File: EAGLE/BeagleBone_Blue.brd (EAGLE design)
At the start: 86.4 x 54.6 mm, 305 parts, among them J2 SERVO_HEADERS_8X, M1 JST_ZH_2, M2 JST_ZH_2, M3 JST_ZH_2, M4 JST_ZH_2, Q1 MOSFET-N, U1 TCAN1051HV, U10 TXS0108ERGYR, U13 EMMC, U2 SN74LV1T126DBVR, U3 TPD4S012DRY, U4 TPD4S012DRY, U5 24LC_32AT-I/OT, U6 SN74LVC1G07_DCK_5, U7 WL1835MODGBMOCT, U9 TXS0108ERGYR, X2 SCHA5B0200, X3 USB1, X4 10118192-0001LF, Y1 24 MHz, Y2 32.768kHz

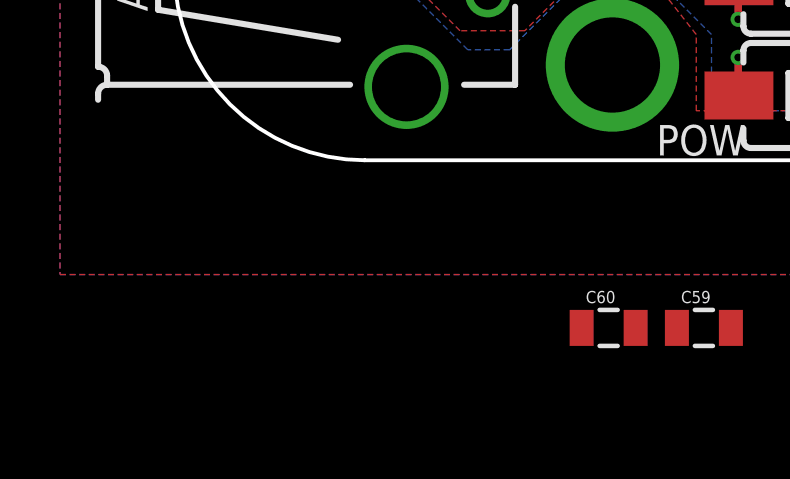
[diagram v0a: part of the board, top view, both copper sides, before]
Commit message: Added TPS2105 power mux for USB1 power.
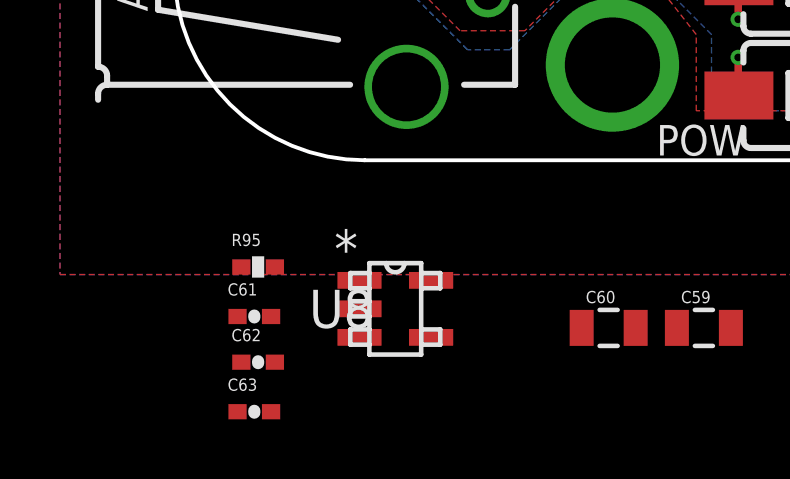
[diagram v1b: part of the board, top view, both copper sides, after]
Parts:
- added C61: 1uF, Strawson_Eagle_Lib:0402-CAP
- added C62, C63: 0.22uF, Strawson_Eagle_Lib:0402-CAP
- added R95: 100K, Strawson_Eagle_Lib:0402-RES
- added U8: TPS2105_DBV_5, BeagleBone_Blue:DBV5
- R119: value 0 -> 0, DNP
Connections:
- net 5.0V: now also C63.1, R95.2, U8.1, U8.5
- net GND: now also C61.1, C62.2, C63.2, R95.1, U8.2
- net SYS_5V: now also C62.1, U8.3
- net USB1_VBUS: now also C61.2, U8.4

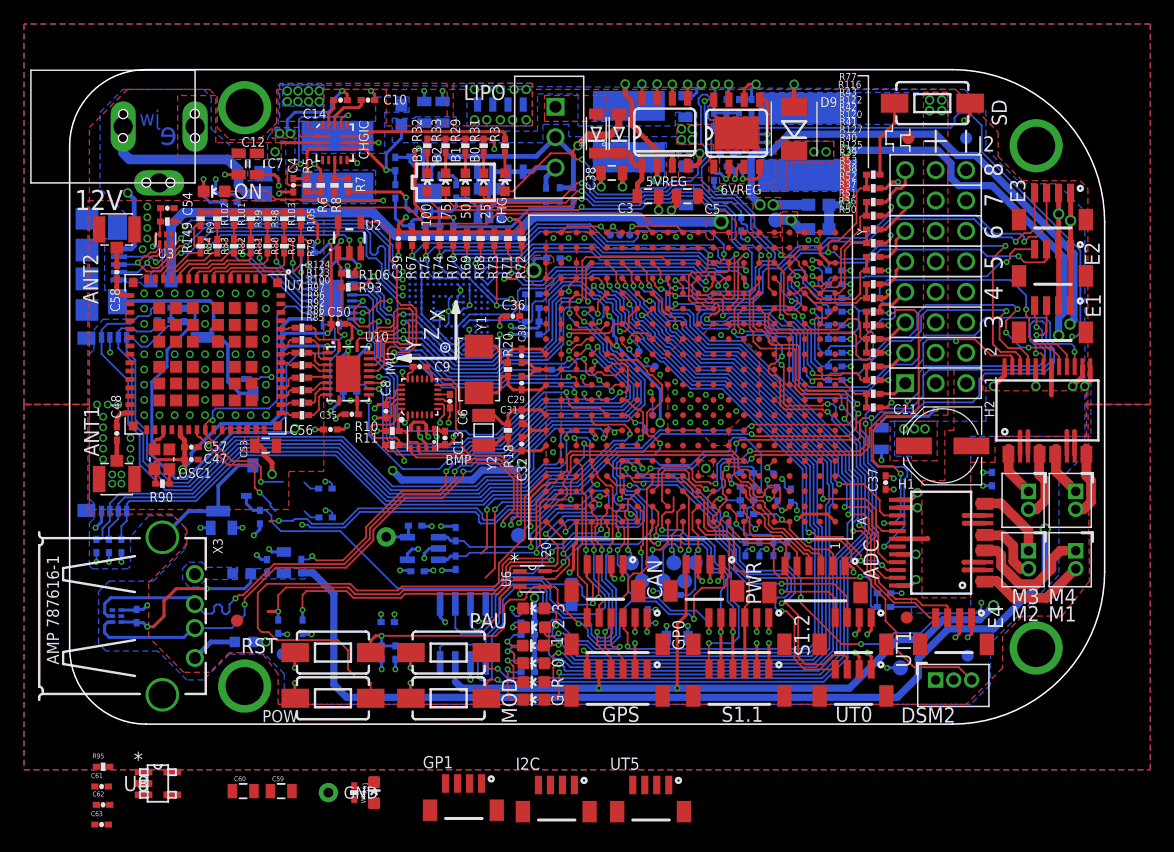
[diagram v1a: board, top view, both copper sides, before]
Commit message: Intermediate commit; Updated layout; Fixed TPS2105 footprint.
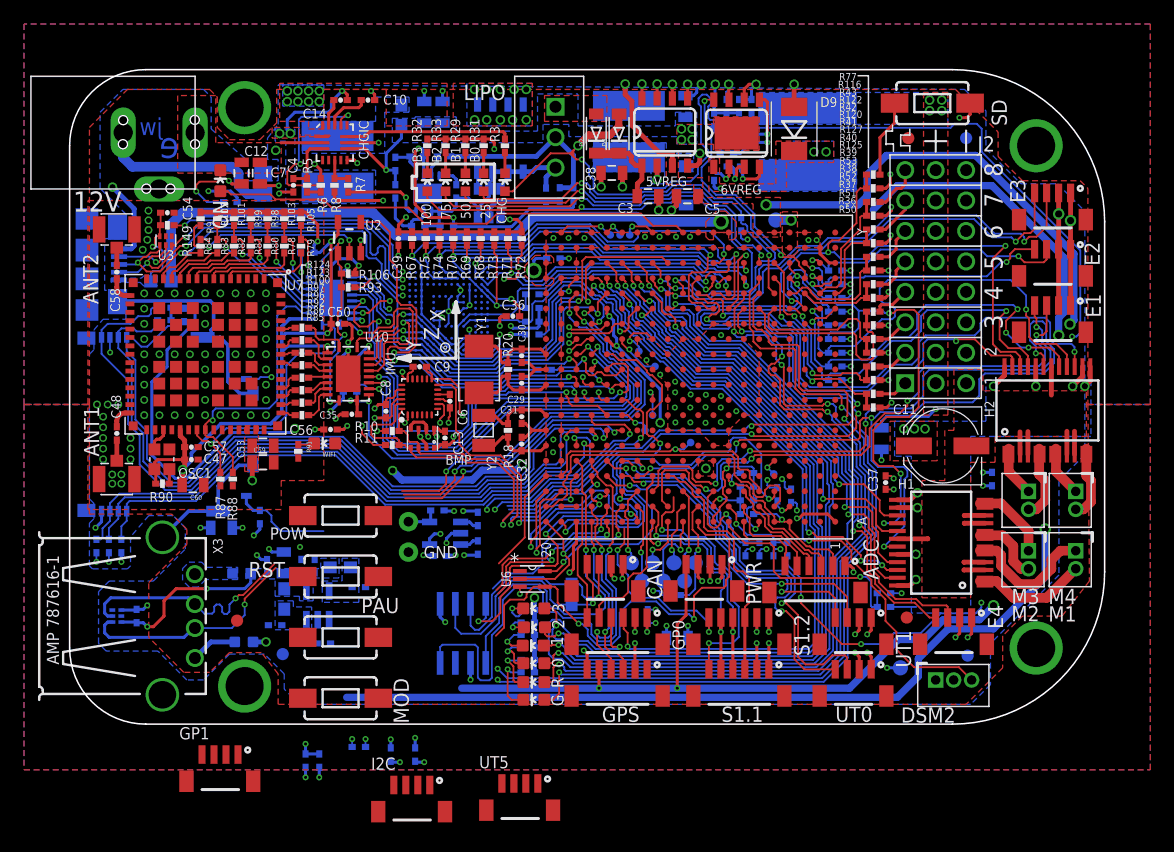
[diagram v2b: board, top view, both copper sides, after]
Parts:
- TP5: value TPSQB1,27 -> TPB0,65; device testpad:B1,27 -> BeagleBone_Blue:BEAGLEBONE_BLUE_B0,65
- moved R121 54.2 mm to (17.9, -44.2), turned to 270 degrees
- moved R119 50.1 mm to (22.6, -41.5), turned to 180 degrees
- moved WIFI 29.4 mm to (21.3, -31.2), turned to 90 degrees
- moved C63 29.2 mm to (24.1, -43.2), flipped to the bottom, turned to 180 degrees
- moved R91 28.9 mm to (19.1, -31.9)
- moved C59 27.5 mm to (16.1, -32.8)
- moved C60 25.9 mm to (10.3, -34.7), turned to 180 degrees
- moved C61 25.6 mm to (20.4, -41.4), flipped to the bottom, turned to 270 degrees
- moved GND 21.1 mm to (28.3, -40.3)
- moved R95 21.1 mm to (21.2, -47.9), flipped to the bottom, turned to 180 degrees
- moved C62 20.7 mm to (17.1, -46.4), flipped to the bottom
- moved GP1 20.5 mm to (13.6, -58.4)
- moved U8 20.0 mm to (20.7, -44.7), flipped to the bottom, turned to 90 degrees
- moved TP5 16.3 mm to (51.8, -31.1)
- moved POW 15.3 mm to (22.6, -37.2)
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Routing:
- net POWER_BTN: track 47.9 -> 8.92 mm
- net USB1_VBUS: track 147.9 -> 124.0 mm, vias 6 -> 4
- net MDIR_2B: track 91.5 -> 69.7 mm, vias 4 -> 3
- net I2C1_SCL: track 35.1 -> 14.0 mm
- net UART5_TX: track 90.8 -> 71.8 mm, vias 4 -> 3
- net I2C1_SDA: track 34.2 -> 16.1 mm
- net N$75: track 44.0 -> 27.9 mm
- net USB1_D_P: track 67.0 -> 53.3 mm
- net USB1_D_N: track 67.0 -> 53.3 mm
- net RESET: track 51.7 -> 40.1 mm
- net N$129: track 47.0 -> 35.4 mm
- net 5.0V: track 144.0 -> 135.9 mm, vias 7 -> 6
- net WL_EN_1V8: track 31.9 -> 24.1 mm, vias 2 -> 1
- net GND: track 239.4 -> 232.2 mm, vias 218 -> 212
- net I2C0_SDA: track 24.1 -> 17.3 mm
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- added copper zone on layer 16, net 5.0V
- added copper zone on layer 16, net SYS_5V

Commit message: Updated placement
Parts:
- moved GP1 28.7 mm to (37.5, -42.5)
- moved UT5 13.9 mm to (37.5, -47.0)
- moved I2C 12.5 mm to (37.5, -51.3)
- moved 2 8.76 mm to (30.0, -46.5)
- moved 0 8.76 mm to (30.0, -49.5)
- moved 1 8.76 mm to (29.9, -48.1)
- moved 3 8.76 mm to (30.0, -45.0)
- moved G 8.76 mm to (30.0, -52.6)
- moved R 8.76 mm to (30.0, -51.1)
- moved R21 8.76 mm to (29.5, -49.3)
- moved R22 8.76 mm to (29.5, -50.3)
- moved R61 8.76 mm to (29.5, -48.2)
- moved R62 8.76 mm to (29.5, -47.2)
- moved R63 8.76 mm to (29.5, -46.1)
- moved R64 8.76 mm to (29.5, -45.1)
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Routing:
- net DCAN1_RX: track 44.6 -> 25.2 mm
- net CANL: track 21.4 -> 8.07 mm
- net DCAN1_SILENT: track 46.5 -> 34.5 mm, vias 3 -> 2
- net CANH: track 19.6 -> 8.70 mm
- net DCAN1_TX: track 30.2 -> 19.7 mm
- net RESET: track 40.1 -> 32.3 mm
- net PAUSE_BTN: track 69.3 -> 76.9 mm, vias 2 -> 1
- net POWER_BTN: track 8.92 -> 2.51 mm
- net I2C1_SDA: track 16.1 -> 9.75 mm
- net I2C1_SCL: track 14.0 -> 7.93 mm
- net N$75: track 27.9 -> 22.9 mm
- net PMIC_PGOOD: track 16.9 -> 14.0 mm
- net 3.3V: track 138.6 -> 136.9 mm, vias 61 -> 60
- net GND: track 232.2 -> 230.8 mm, vias 212 -> 211
- net VDD_RTC: track 20.3 -> 19.3 mm
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
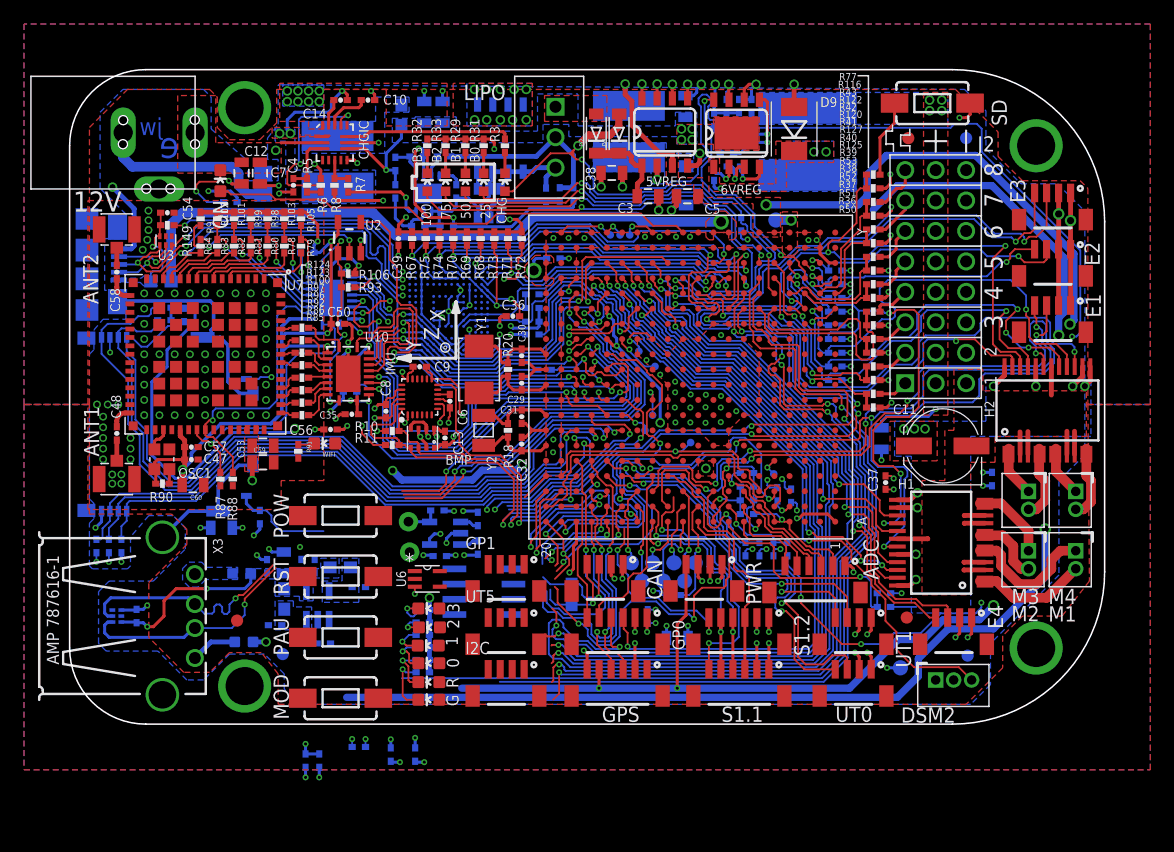
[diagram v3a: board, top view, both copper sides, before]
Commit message: Updated schematics:  removed some test points; changed GPIO 1 connector to 6 pin JST; Updated EQEP layout.
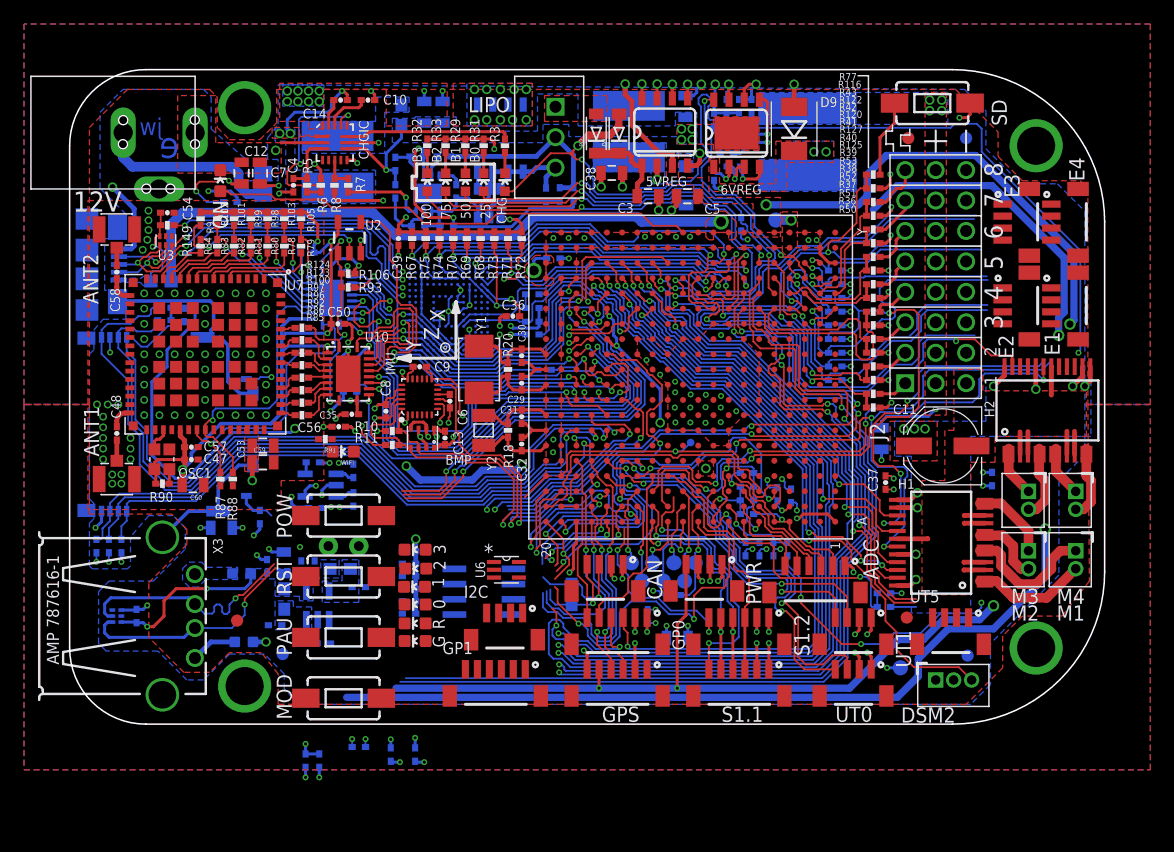
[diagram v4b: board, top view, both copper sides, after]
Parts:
- removed TP11, TP2, TP3, TP4, TP6, TP7, TP8, TP9: TPB0,65, BeagleBone_Blue:BEAGLEBONE_BLUE_B0,65
- GP1: value JST_SH_4 -> JST_SH_6; device Strawson_Eagle_Lib:JST_SH_4_SMD -> Strawson_Eagle_Lib:JST_SH_6
- moved UT5 37.1 mm to (74.5, -47.0)
- moved E4 36.3 mm to (83.2, -11.7), turned to 90 degrees
- moved R58 11.1 mm to (20.3, -32.8)
- moved R2 11.1 mm to (23.7, -35.9)
- moved R23 11.1 mm to (23.7, -33.5)
- moved U5 11.1 mm to (20.9, -34.7)
- moved C28 11.1 mm to (20.5, -36.6)
- moved GP1 8.71 mm to (33.0, -50.0)
- moved WP 6.98 mm to (21.6, -39.8)
- moved U6 6.65 mm to (36.4, -41.7)
- moved 0 5.03 mm to (28.8, -44.6)
- moved 1 5.03 mm to (28.8, -43.2)
- moved 2 5.03 mm to (28.9, -41.6)
- moved 3 5.03 mm to (28.8, -40.1)
- moved G 5.03 mm to (28.8, -47.7)
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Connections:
- net GPIO_0_0 renamed GPIO1_25
- net GPIO_0_1 renamed GPIO1_17
- net GPIO_0_2 renamed GPIO3_20
- net GPIO_0_3 renamed GPIO3_17
- net GPIO_1_0 renamed GPIO3_2
- net GPIO_1_1 renamed GPIO3_1
- removed net N$19: SIP.Y13, TP7.TP
- removed net N$21: SIP.Y16, TP9.TP
- removed net N$23: SIP.Y19, TP11.TP
- removed net N$72: SIP.N15, TP2.TP
- removed net N$73: SIP.J13, TP3.TP
- removed net N$76: SIP.H15, TP4.TP
- removed net N$78: SIP.N13, TP6.TP
- removed net N$80: SIP.E5, TP8.TP
- net LED_GRN: now also GP1.5
- net LED_RED: now also GP1.6
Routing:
- net MDIR_3B: track 44.8 -> 30.6 mm, vias 3 -> 2
- net PWM_2B: track 44.6 -> 31.8 mm, vias 2 -> 1
- net MDIR_4B: track 36.6 -> 24.5 mm, vias 2 -> 1
- net GND: track 230.8 -> 219.0 mm, vias 211 -> 208
- net MDIR_4A: track 34.4 -> 23.3 mm, vias 4 -> 1
- net EQEP_2A: track 40.5 -> 30.2 mm, vias 2 -> 1
- net 3.3V: track 136.9 -> 127.2 mm, vias 60 -> 58
- net EQEP_2B: track 39.2 -> 29.9 mm, vias 2 -> 1
- net MOT_STBY: track 65.2 -> 56.0 mm
- net MODE_BTN: track 70.8 -> 79.1 mm
- net MDIR_3A: track 32.5 -> 24.4 mm, vias 2 -> 1
- net EQEP_1A: track 23.0 -> 16.1 mm, vias 2 -> 1
- net EQEP_0A: track 49.3 -> 43.8 mm, vias 4 -> 3
- net 5.0V: track 135.9 -> 141.4 mm
- net EQEP_0B: track 48.7 -> 43.4 mm, vias 4 -> 3
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
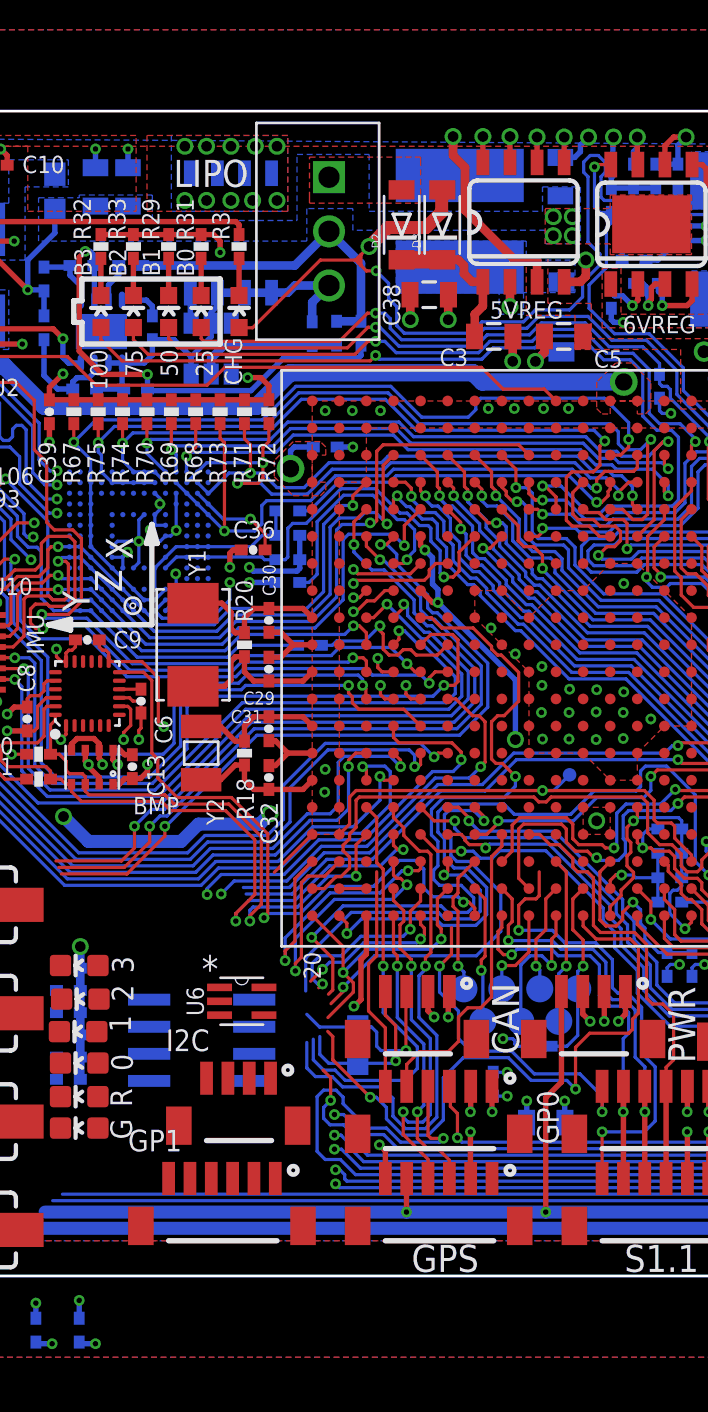
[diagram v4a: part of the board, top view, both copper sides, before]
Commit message: Updated L1, Q1 for DFM issues from manufacturer.
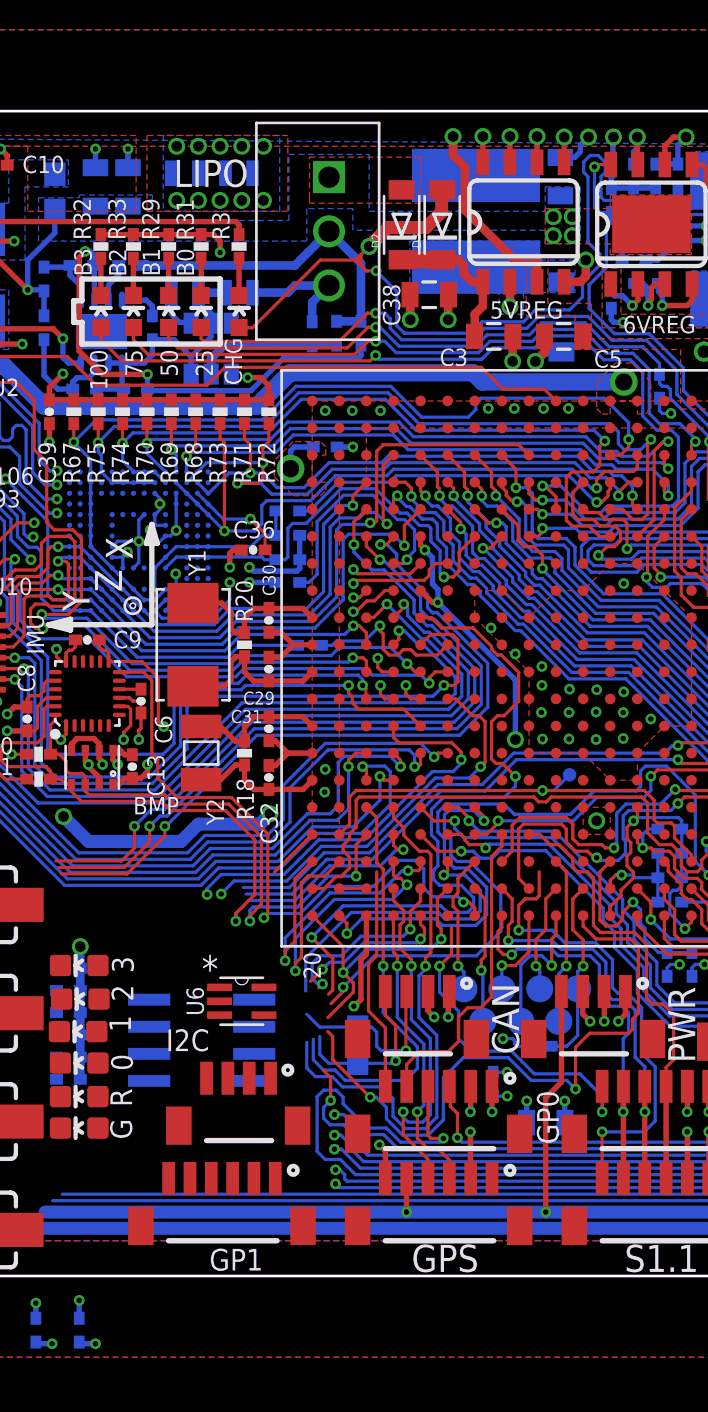
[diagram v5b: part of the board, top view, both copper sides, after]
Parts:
- moved Q1 0.89 mm to (35.1, -5.71)
- moved L1 0.76 mm to (47.6, -5.14)
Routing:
- net BATT_MINUS: track 19.3 -> 20.4 mm
- net 5.0V: track 141.4 -> 142.2 mm
- net DO: track 1.44 -> 2.11 mm
